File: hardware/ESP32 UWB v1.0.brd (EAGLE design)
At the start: 72 x 32.6 mm, 54 parts, among them IC1 CP2104, J2 HEADER-12P-2.54, J3 USB-MICRO-5P, Q3 S8050, Q4 S8050, U1 ESP32-WROVER, U2 ME6217C33M5G, U3 ESP-WROOM-32, U4 LD1117/3.3v, U5 DWM1000

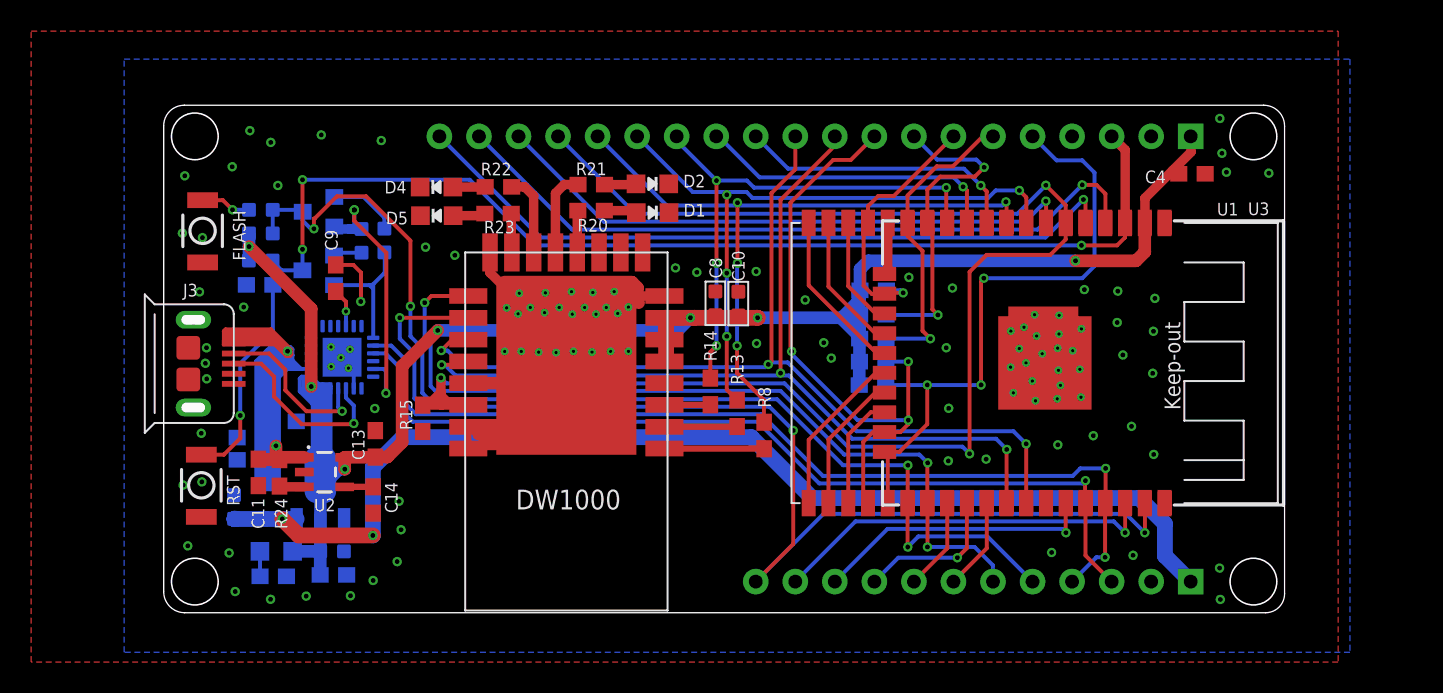
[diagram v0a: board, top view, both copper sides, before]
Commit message: swaped ESP module to ESP32-C3-MINI
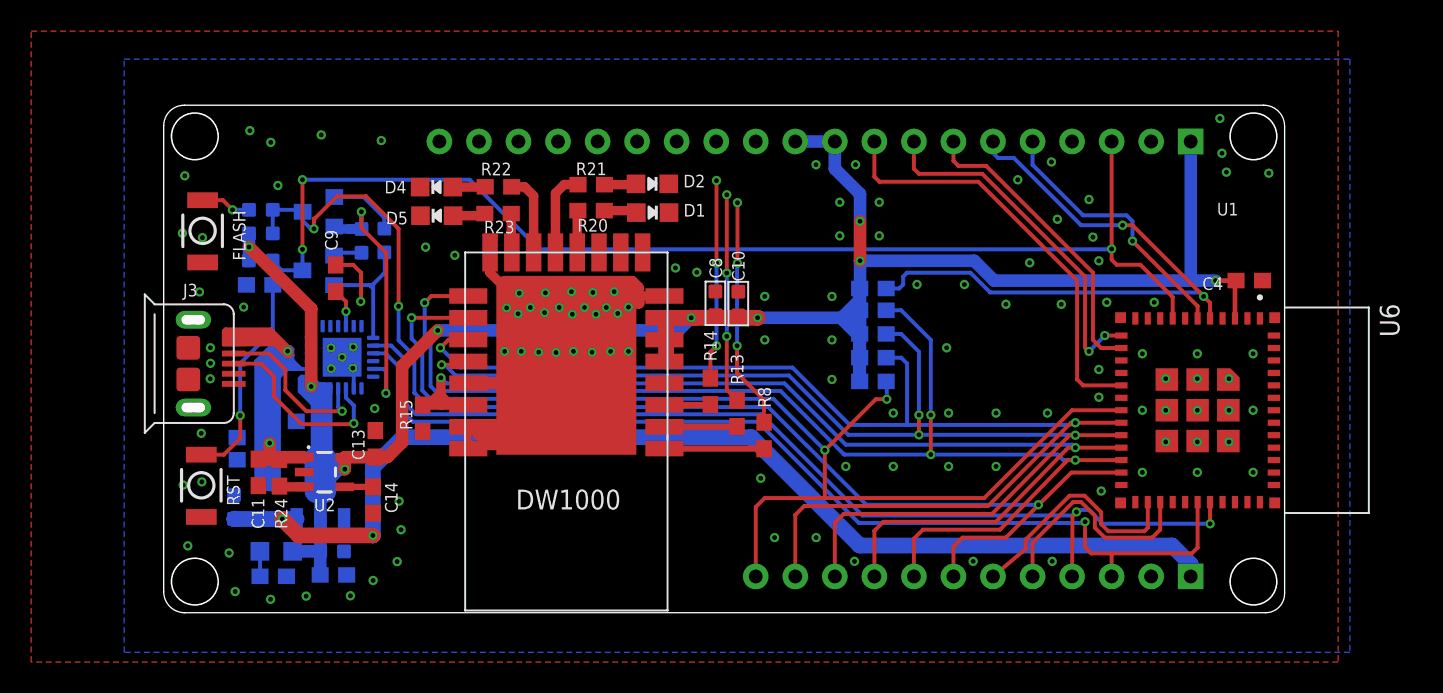
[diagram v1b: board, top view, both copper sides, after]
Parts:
- removed U1: ESP32-WROVER, ESP32-Wrover:ESP32-WROVER
- removed U3: ESP-WROOM-32, esp32:ESP-WROOM-32
- added U6: ESP32-C3-MINI-1-N4, ESP32-C3-MINI-1-N4:XCVR_ESP32-C3-MINI-1-N4
- moved C4 7.79 mm to (69.7, 21.3)
- moved R19 6.20 mm to (45.6, 20.8)
- moved R16 5.85 mm to (45.6, 14.9)
- moved R18 3.30 mm to (45.6, 19.4)
- moved R17 1.23 mm to (45.6, 17.9)
- moved R6 1.23 mm to (45.6, 16.4)
- moved J1 0.33 mm to (40.6, 30.3)
- moved J2 0.33 mm to (52.0, 2.33)
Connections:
- removed net CLK: U1.CLK, U3.20
- removed net CMD: U1.CMD, U3.19
- removed net IO12/MISO: J1.6, R6.2, U1.IO12, U3.14
- removed net IO13/MOSI: J1.7, R16.2, U1.IO13, U3.16
- removed net IO14/SCLK: J1.8, R17.2, U1.IO14, U3.13
- removed net IO15/NSS: J1.9, R18.2, U1.IO15, U3.23
- removed net IO16: J2.8, U1.NC1, U3.27
- removed net IO17: J2.9, U1.NC2, U3.28
- removed net IO21/RES: J2.10, U1.IO21, U3.33
- removed net IO22/DC: J2.11, U1.IO22, U3.36
- removed net IO23: J2.12, U1.IO23, U3.37, U5.SPIMOSI
- removed net IO25: J1.12, U1.IO25, U3.10
- removed net IO26: J1.13, U1.IO26, U3.11
- removed net IO34: J1.17, R15.1, U1.IO34, U3.6, U5.IRQ/GPIO8
- removed net IO35: J1.18, U1.IO35, U3.7
- removed net IO36/SVP: J1.19, U1.SENSOR_VP, U3.4
- removed net IO39/SVN: J1.20, U1.SENSOR_VN, U3.5
- removed net IO4: J2.6, U1.IO4, U3.26, U5.SPICSN
- removed net IO5: J2.7, U1.IO5, U3.29
- removed net NC: U1.NC0, U3.32
- removed net SD0: U1.SD0, U3.21
- removed net SD1: U1.SD1, U3.22
- removed net SD2: U1.SD2, U3.17
- removed net SD3: U1.SD3, U3.18
- new net IO1: J1.7, U6.13
- new net IO10: J1.9, U6.16
- new net IO3: J1.5, U6.6
- new net IO4/MOSI: J2.12, R16.2, U5.SPIMOSI, U6.18
- new net IO5/MISO: J2.11, R6.2, U5.SPIMISO, U6.19
- new net IO6/SCLK: J2.10, R17.2, U5.SPICLK, U6.20
- new net IO7: J2.9, R15.1, U5.IRQ/GPIO8, U6.21
- new net IO8/CS: J2.8, R18.2, U5.SPICSN, U6.22
- new net IO9: J2.7, Q3.3, R10.2, R7.1, U6.23
- net +3V3: now also J1.10, J1.11, U6.3; no longer U1.VDD33, U3.2
- net GND: now also J1.12, J1.13, J1.14, J1.15, J1.16, J1.17, J1.18, J1.19, J1.20, U6.1, U6.11, U6.14, U6.2, U6.36, U6.37, U6.38, U6.39, U6.40, U6.41, U6.42, U6.43, U6.44, U6.45, U6.46, U6.47, U6.48, U6.49_1, U6.49_2, U6.49_3, U6.49_4, U6.49_5, U6.49_6, U6.49_7, U6.49_8, U6.49_9, U6.50, U6.51, U6.52, U6.53; no longer U1.GND, U1.GND2, U1.GND3, U1.GND_2, U3.1, U3.15, U3.38, U3.GND
- net IO0: now also J1.8, U6.12; no longer J2.5, Q3.3, R10.2, R7.1, U1.IO0, U3.25
- net IO18: now also J2.6, U6.26; no longer J1.10, U1.IO18, U3.30, U5.SPICLK
- net IO19: now also J2.5, U6.27; no longer J1.11, U1.IO19, U3.31, U5.SPIMISO
- net IO2: now also J1.6, U6.5; no longer J1.5, U1.IO2, U3.24
- net IO27: no longer J1.14, U1.IO27, U3.12
- net IO32: no longer J1.15, U1.IO32, U3.8
- net IO33: no longer J1.16, U1.IO33, U3.9
- net RESET: now also U6.8; no longer U1.EN, U3.3
- net RXD: now also U6.30; no longer U1.RXD0, U3.34
- net TXD: now also U6.31; no longer U1.TXD0, U3.35
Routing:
- net IO34: track 99.4 -> 0.00 mm, vias 3 -> 0
- net IO9: track 0.00 -> 81.4 mm, vias 0 -> 3
- net IO8/CS: track 0.00 -> 80.8 mm, vias 0 -> 4
- net IO5/MISO: track 0.00 -> 77.7 mm, vias 0 -> 2
- net IO6/SCLK: track 0.00 -> 76.5 mm, vias 0 -> 4
- net IO4/MOSI: track 0.00 -> 76.1 mm, vias 0 -> 3
- net IO23: track 75.1 -> 0.00 mm, vias 3 -> 0
- net IO7: track 0.00 -> 70.1 mm, vias 0 -> 2
- net IO4: track 53.6 -> 0.00 mm, vias 3 -> 0
- net IO0: track 71.7 -> 23.0 mm, vias 4 -> 2
- net IO19: track 61.5 -> 14.8 mm, vias 3 -> 0
- net IO39/SVN: track 46.6 -> 0.00 mm, vias 1 -> 0
- net IO36/SVP: track 46.0 -> 0.00 mm, vias 1 -> 0
- net IO18: track 60.6 -> 15.5 mm, vias 3 -> 0
- net +3V3: track 153.6 -> 194.6 mm, vias 7 -> 9
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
